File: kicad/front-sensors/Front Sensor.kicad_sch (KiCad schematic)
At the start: 0 parts

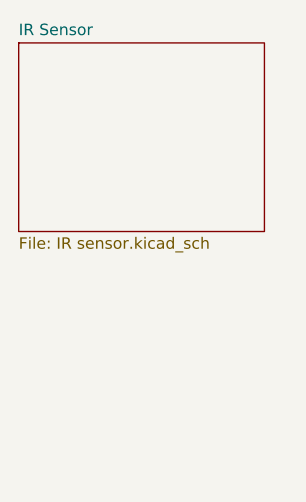
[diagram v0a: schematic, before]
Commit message: Side sensor VL6180
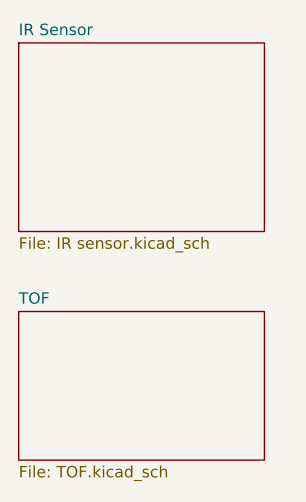
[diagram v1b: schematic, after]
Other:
- added sheet TOF (TOF.kicad_sch)
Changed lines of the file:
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@@
+		)
+	)
+	(sheet
+		(at 106.68 107.315)
+		(size 27.305 16.51)
+		(exclude_from_sim no)
+		(in_bom yes)
+		(on_board yes)
+		(dnp no)
+		(fields_autoplaced yes)
+		(stroke
+			(width 0.1524)
+			(type solid)
+		)
+		(fill
+			(color 0 0 0 0)
+		)
+		(property "Sheetname" "TOF"
+			(at 106.68 106.6034 0)
+			(show_name no)
+			(do_not_autoplace no)
+			(effects
+				(font
+					(size 1.27 1.27)
+				)
+				(justify left bottom)
+			)
+		)
+		(property "Sheetfile" "TOF.kicad_sch"
+			(at 106.68 124.4096 0)
+			(show_name no)
+			(do_not_autoplace no)
+			(effects
+				(font
+					(size 1.27 1.27)
+				)
+				(justify left top)
+			)
+		)
+		(instances
+			(project "Front Sensor"
+				(path "/b1780c3e-7100-4df4-97c9-2fd6186fb125"
+					(page "3")
+				)
+			)
 		)
 	)
